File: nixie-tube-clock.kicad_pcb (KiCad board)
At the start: 2 copper layers, 131 parts, among them IC1 TPS61041DBVR, IC2 UCC3803DTR, J5 USB4105-GF-A, J7 DEBUG, Q1 MMBT42, Q2 FDS2672CT, SW1 SW_SPST, U1 CD40109BPW, U2 W25Q32JV, U3 RP2350A, U4 MCP1702T-3302E_CB, U5 CD40109BPW, U6 HV5122PG-G, U7 HV5122PG-G, U8 DS3231M, X1 IQXO-791

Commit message: Add global labels for nets spanning several sheets
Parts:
- moved D12 240.0 mm to (255.5, 98.7)
- moved D11 216.6 mm to (230.1, 98.7)
- moved D10 193.9 mm to (204.7, 98.7)
- moved N6 191.6 mm to (255.5, 98.7)
- moved N4 185.5 mm to (230.1, 98.7)
- moved N2 179.4 mm to (204.7, 98.7)
- moved D9 171.9 mm to (178.8, 99.1)
- moved D8 152.3 mm to (154.0, 99.1)
- moved D7 135.9 mm to (130.6, 99.1)
- moved N5 129.6 mm to (178.8, 99.1)
- moved N3 124.8 mm to (154.0, 99.1)
- moved N1 121.3 mm to (130.6, 99.1)
- moved U6 28.3 mm to (112.6, 106.1)
- moved C34 12.9 mm to (86.4, 46.5), turned to -90 degrees
- moved U8 5.59 mm to (94.0, 48.3)
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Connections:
- N1 pad 1: /nixie_tubes/N1.1 -> N1.1
- U6 pad 36: /nixie_tubes_driver/N1.1 -> N1.1

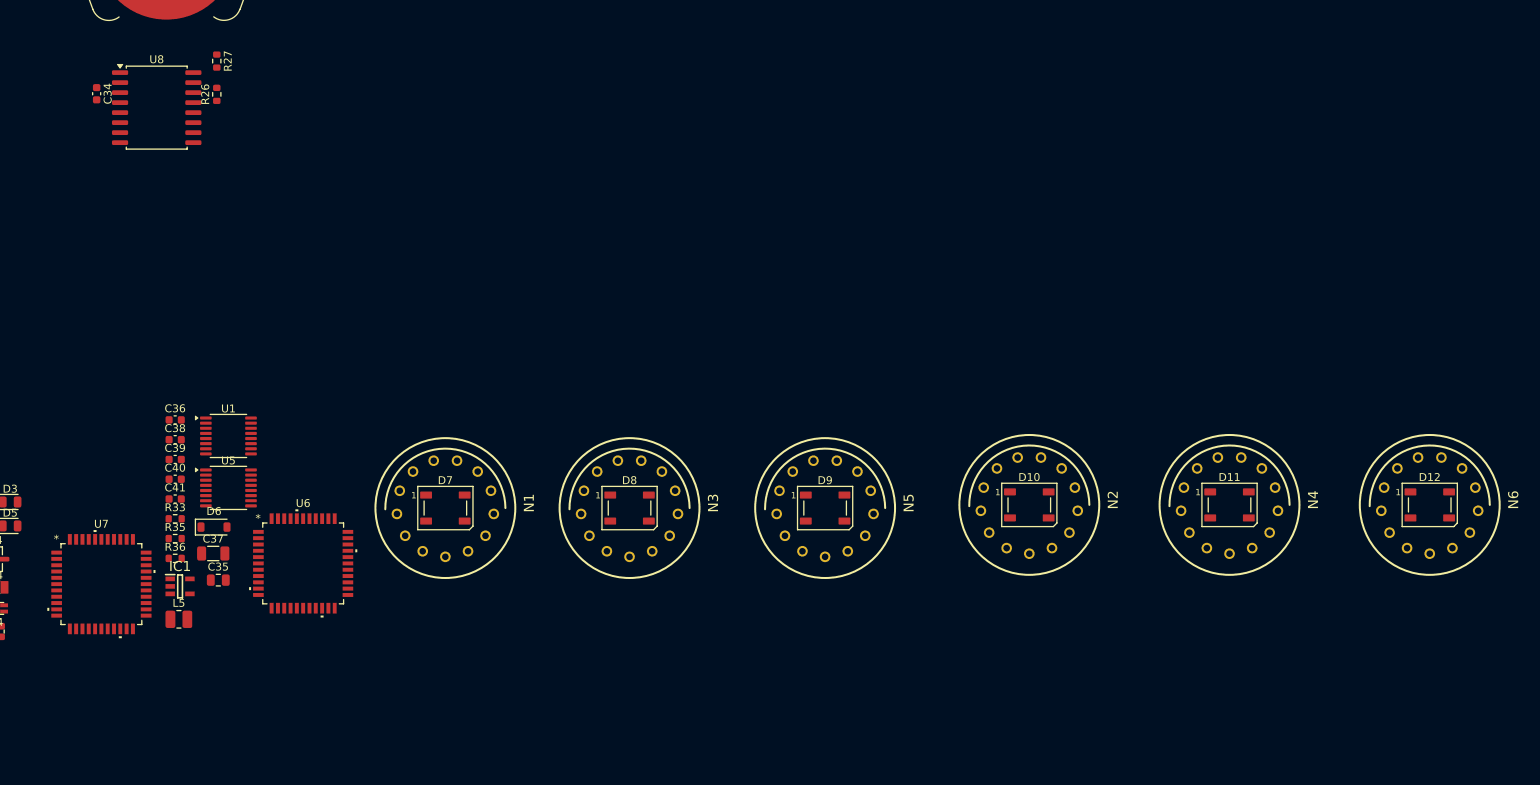
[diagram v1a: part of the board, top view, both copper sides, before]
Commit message: Modify nixie tube nets for easier layout
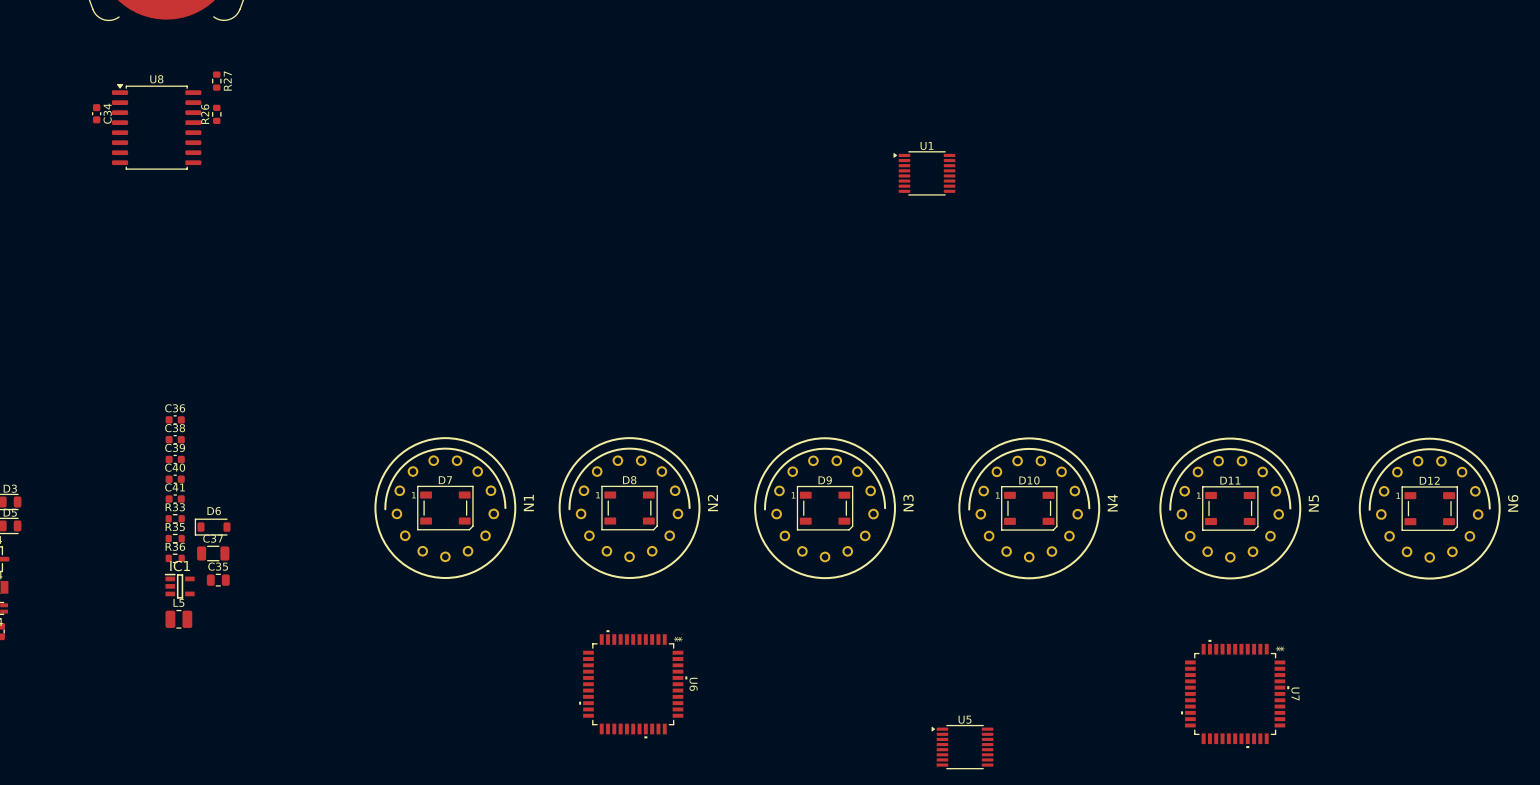
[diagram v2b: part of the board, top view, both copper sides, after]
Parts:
- moved U7 144.5 mm to (230.8, 122.6), turned to -90 degrees
- moved U5 99.1 mm to (196.5, 129.4)
- moved U1 94.7 mm to (191.7, 56.6)
- moved N5 51.4 mm to (230.2, 99.1)
- moved N2 50.7 mm to (154.0, 99.1)
- moved U6 44.6 mm to (154.4, 121.4), turned to -90 degrees
- moved N4 25.4 mm to (204.7, 99.1)
- moved N3 24.8 mm to (178.8, 99.1)
- moved R27 2.54 mm to (101.6, 44.9)
- moved C34 2.54 mm to (86.4, 49.0)
- moved R26 2.54 mm to (101.6, 49.1)
- moved U8 2.54 mm to (94.0, 50.8)
- moved D12 0.47 mm to (255.5, 99.1)
- moved N6 0.47 mm to (255.5, 99.1)
- moved D11 0.46 mm to (230.2, 99.1)
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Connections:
- D7 pad 4: /nixie_tubes/LED_LOGIC_5V -> LED_LOGIC_5V
- N1 pad 0: /nixie_tubes/N1.0 -> N1.0
- N1 pad 2: /nixie_tubes/N1.2 -> N1.2
- N1 pad 3: /nixie_tubes/N1.3 -> N1.3
- N1 pad 4: /nixie_tubes/N1.4 -> N1.4
- N1 pad 5: /nixie_tubes/N1.5 -> N1.5
- N1 pad 6: /nixie_tubes/N1.6 -> N1.6
- N1 pad 7: /nixie_tubes/N1.7 -> N1.7
- N1 pad 8: /nixie_tubes/N1.8 -> N1.8
- N1 pad 9: /nixie_tubes/N1.9 -> N1.9
- N2 pad 0: /nixie_tubes/N2.0 -> N2.0
- N2 pad 1: /nixie_tubes/N2.1 -> N2.1
- N2 pad 2: /nixie_tubes/N2.2 -> N2.2
- N2 pad 3: /nixie_tubes/N2.3 -> N2.3
- N2 pad 4: /nixie_tubes/N2.4 -> N2.4
- N2 pad 5: /nixie_tubes/N2.5 -> N2.5
- N2 pad 6: /nixie_tubes/N2.6 -> N2.6
- N2 pad 7: /nixie_tubes/N2.7 -> N2.7
- N2 pad 8: /nixie_tubes/N2.8 -> N2.8
- N2 pad 9: /nixie_tubes/N2.9 -> N2.9
- N3 pad 0: /nixie_tubes/N3.0 -> N3.0
- N3 pad 1: /nixie_tubes/N3.1 -> N3.1
- N3 pad 2: /nixie_tubes/N3.2 -> N3.2
- N3 pad 3: /nixie_tubes/N3.3 -> N3.3
- N3 pad 4: /nixie_tubes/N3.4 -> N3.4
- N3 pad 5: /nixie_tubes/N3.5 -> N3.5
- N3 pad 6: /nixie_tubes/N3.6 -> N3.6
- N3 pad 7: /nixie_tubes/N3.7 -> N3.7
- N3 pad 8: /nixie_tubes/N3.8 -> N3.8
- N3 pad 9: /nixie_tubes/N3.9 -> N3.9
- N4 pad 0: /nixie_tubes/N4.0 -> N4.0
- N4 pad 1: /nixie_tubes/N4.1 -> N4.1
- N4 pad 2: /nixie_tubes/N4.2 -> N4.2
- N4 pad 3: /nixie_tubes/N4.3 -> N4.3
- N4 pad 4: /nixie_tubes/N4.4 -> N4.4
- N4 pad 5: /nixie_tubes/N4.5 -> N4.5
- N4 pad 6: /nixie_tubes/N4.6 -> N4.6
- N4 pad 7: /nixie_tubes/N4.7 -> N4.7
- N4 pad 8: /nixie_tubes/N4.8 -> N4.8
- N4 pad 9: /nixie_tubes/N4.9 -> N4.9
- N5 pad 0: /nixie_tubes/N5.0 -> N5.0
- N5 pad 1: /nixie_tubes/N5.1 -> N5.1
- N5 pad 2: /nixie_tubes/N5.2 -> N5.2
- N5 pad 3: /nixie_tubes/N5.3 -> N5.3
- N5 pad 4: /nixie_tubes/N5.4 -> N5.4
- N5 pad 5: /nixie_tubes/N5.5 -> N5.5
- N5 pad 6: /nixie_tubes/N5.6 -> N5.6
- N5 pad 7: /nixie_tubes/N5.7 -> N5.7
- N5 pad 8: /nixie_tubes/N5.8 -> N5.8
- N5 pad 9: /nixie_tubes/N5.9 -> N5.9
- N6 pad 0: /nixie_tubes/N6.0 -> N6.0
- N6 pad 1: /nixie_tubes/N6.1 -> N6.1
- N6 pad 2: /nixie_tubes/N6.2 -> N6.2
- N6 pad 3: /nixie_tubes/N6.3 -> N6.3
- N6 pad 4: /nixie_tubes/N6.4 -> N6.4
- N6 pad 5: /nixie_tubes/N6.5 -> N6.5
- N6 pad 6: /nixie_tubes/N6.6 -> N6.6
- N6 pad 7: /nixie_tubes/N6.7 -> N6.7
- N6 pad 8: /nixie_tubes/N6.8 -> N6.8
- N6 pad 9: /nixie_tubes/N6.9 -> N6.9
- R26 pad 2: /real_time_clock/RTC_SDA -> RTC_SDA
- R27 pad 2: /real_time_clock/RTC_SCL -> RTC_SCL
- U1 pad 3: /nixie_tubes_driver/LED_LOGIC_3V3 -> LED_LOGIC_3V3
- U1 pad 4: /nixie_tubes_driver/LED_LOGIC_5V -> LED_LOGIC_5V
- U3 pad 14: /microcontroller/SR_CLK_3V3 -> SR_CLK_3V3
- U3 pad 15: /microcontroller/SR_DATA_IN_3V3 -> SR_DATA_IN_3V3
- U3 pad 16: /microcontroller/SR_STR_3V3 -> SR_STR_3V3
- U3 pad 17: /microcontroller/SR_OE_3V3 -> SR_OE_3V3
- U3 pad 18: /microcontroller/LED_LOGIC_3V3 -> LED_LOGIC_3V3
- U3 pad 2: /microcontroller/RTC_SDA -> RTC_SDA
- U3 pad 3: /microcontroller/RTC_SCL -> RTC_SCL
- U5 pad 10: /nixie_tubes_driver/SR_STR_3V3 -> SR_STR_3V3
- U5 pad 14: /nixie_tubes_driver/SR_OE_3V3 -> SR_OE_3V3
- U5 pad 3: /nixie_tubes_driver/SR_DATA_IN_3V3 -> SR_DATA_IN_3V3
- U5 pad 6: /nixie_tubes_driver/SR_CLK_3V3 -> SR_CLK_3V3
- U6 pad 1: /nixie_tubes_driver/N2.0 -> N2.1
- U6 pad 10: /nixie_tubes_driver/N2.9 -> N2.0
- U6 pad 11: /nixie_tubes_driver/N3.0 -> N1.1
- U6 pad 12: /nixie_tubes_driver/N3.1 -> N1.2
- U6 pad 13: /nixie_tubes_driver/N3.2 -> N1.3
- U6 pad 14: /nixie_tubes_driver/N3.3 -> N1.4
- U6 pad 15: /nixie_tubes_driver/N3.4 -> N1.5
- U6 pad 16: /nixie_tubes_driver/N3.5 -> N1.6
- U6 pad 17: /nixie_tubes_driver/N3.6 -> N1.7
- U6 pad 18: /nixie_tubes_driver/N3.7 -> N1.8
- U6 pad 19: /nixie_tubes_driver/N3.8 -> N1.9
- U6 pad 2: /nixie_tubes_driver/N2.1 -> N2.2
- U6 pad 20: /nixie_tubes_driver/N3.9 -> N1.0
- U6 pad 3: /nixie_tubes_driver/N2.2 -> N2.3
- U6 pad 35: /nixie_tubes_driver/N1.0 -> N3.1
- U6 pad 36: N1.1 -> N3.2
- U6 pad 37: /nixie_tubes_driver/N1.2 -> N3.3
- U6 pad 38: /nixie_tubes_driver/N1.3 -> N3.4
- U6 pad 39: /nixie_tubes_driver/N1.4 -> N3.5
- U6 pad 4: /nixie_tubes_driver/N2.3 -> N2.4
- U6 pad 40: /nixie_tubes_driver/N1.5 -> N3.6
- U6 pad 41: /nixie_tubes_driver/N1.6 -> N3.7
- U6 pad 42: /nixie_tubes_driver/N1.7 -> N3.8
- U6 pad 43: /nixie_tubes_driver/N1.8 -> N3.9
- U6 pad 44: /nixie_tubes_driver/N1.9 -> N3.0
- U6 pad 5: /nixie_tubes_driver/N2.4 -> N2.5
- U6 pad 6: /nixie_tubes_driver/N2.5 -> N2.6
- U6 pad 7: /nixie_tubes_driver/N2.6 -> N2.7
- U6 pad 8: /nixie_tubes_driver/N2.7 -> N2.8
- U6 pad 9: /nixie_tubes_driver/N2.8 -> N2.9
- U7 pad 1: /nixie_tubes_driver/N5.0 -> N5.1
- U7 pad 10: /nixie_tubes_driver/N5.9 -> N5.0
- U7 pad 11: /nixie_tubes_driver/N6.0 -> N4.1
- U7 pad 12: /nixie_tubes_driver/N6.1 -> N4.2
- U7 pad 13: /nixie_tubes_driver/N6.2 -> N4.3
- U7 pad 14: /nixie_tubes_driver/N6.3 -> N4.4
- U7 pad 15: /nixie_tubes_driver/N6.4 -> N4.5
- U7 pad 16: /nixie_tubes_driver/N6.5 -> N4.6
- U7 pad 17: /nixie_tubes_driver/N6.6 -> N4.7
- U7 pad 18: /nixie_tubes_driver/N6.7 -> N4.8
- U7 pad 19: /nixie_tubes_driver/N6.8 -> N4.9
- U7 pad 2: /nixie_tubes_driver/N5.1 -> N5.2
- U7 pad 20: /nixie_tubes_driver/N6.9 -> N4.0
- U7 pad 3: /nixie_tubes_driver/N5.2 -> N5.3
- U7 pad 35: /nixie_tubes_driver/N4.0 -> N6.1
- U7 pad 36: /nixie_tubes_driver/N4.1 -> N6.2
- U7 pad 37: /nixie_tubes_driver/N4.2 -> N6.3
- U7 pad 38: /nixie_tubes_driver/N4.3 -> N6.4
- U7 pad 39: /nixie_tubes_driver/N4.4 -> N6.5
- U7 pad 4: /nixie_tubes_driver/N5.3 -> N5.4
- U7 pad 40: /nixie_tubes_driver/N4.5 -> N6.6
- U7 pad 41: /nixie_tubes_driver/N4.6 -> N6.7
- U7 pad 42: /nixie_tubes_driver/N4.7 -> N6.8
- U7 pad 43: /nixie_tubes_driver/N4.8 -> N6.9
- U7 pad 44: /nixie_tubes_driver/N4.9 -> N6.0
- U7 pad 5: /nixie_tubes_driver/N5.4 -> N5.5
- U7 pad 6: /nixie_tubes_driver/N5.5 -> N5.6
- U7 pad 7: /nixie_tubes_driver/N5.6 -> N5.7
- U7 pad 8: /nixie_tubes_driver/N5.7 -> N5.8
- U7 pad 9: /nixie_tubes_driver/N5.8 -> N5.9
- U8 pad 15: /real_time_clock/RTC_SDA -> RTC_SDA
- U8 pad 16: /real_time_clock/RTC_SCL -> RTC_SCL

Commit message: Begin positioning and grouping components
Add bypass caps to level shifters Vdd
Rearrange pins on shift register
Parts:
- added C48: 0.1uF, Capacitor_SMD:C_0603_1608Metric, F.Cu at (195.8, 62.7)
- added C49: 0.1uF, Capacitor_SMD:C_0603_1608Metric, F.Cu at (111.5, 105.4)
- added H1: MountingHole, MountingHole:MountingHole_3.2mm_M3, F.Cu at (84.0, 26.4)
- added H2: MountingHole, MountingHole:MountingHole_3.2mm_M3, F.Cu at (84.0, 34.3)
- added H3: MountingHole, MountingHole:MountingHole_3.2mm_M3, F.Cu at (84.0, 42.3)
- added H4: MountingHole, MountingHole:MountingHole_3.2mm_M3, F.Cu at (84.0, 50.2)
- moved R34 229.8 mm to (255.6, 114.9), turned to 90 degrees
- moved R42 225.6 mm to (255.6, 120.0), turned to 90 degrees
- moved C47 212.1 mm to (257.3, 102.6), turned to 180 degrees
- moved R32 205.4 mm to (230.1, 115.1), turned to 90 degrees
- moved R41 201.5 mm to (230.1, 120.1), turned to 90 degrees
- moved C46 187.6 mm to (231.9, 102.6), turned to 180 degrees
- moved R31 181.6 mm to (204.7, 115.1), turned to 90 degrees
- moved R40 178.0 mm to (204.7, 120.1), turned to 90 degrees
- moved D4 165.6 mm to (220.4, 35.2), turned to -90 degrees
- moved J5 164.1 mm to (191.5, 22.3), turned to 180 degrees
- moved R21 163.8 mm to (217.4, 33.0)
- moved R22 163.8 mm to (217.4, 35.5)
- moved R23 163.8 mm to (217.4, 38.0)
- moved C45 163.3 mm to (206.5, 102.6), turned to 180 degrees
- moved C34 162.3 mm to (248.7, 47.7), turned to 90 degrees
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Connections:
- U6 pad 1: N2.1 -> N2.0
- U6 pad 10: N2.0 -> N2.1
- U6 pad 11: N1.1 -> N3.0
- U6 pad 12: N1.2 -> N3.9
- U6 pad 13: N1.3 -> N3.8
- U6 pad 14: N1.4 -> N3.7
- U6 pad 15: N1.5 -> N3.6
- U6 pad 16: N1.6 -> N3.5
- U6 pad 17: N1.7 -> N3.4
- U6 pad 18: N1.8 -> N3.3
- U6 pad 19: N1.9 -> N3.2
- U6 pad 2: N2.2 -> N2.9
- U6 pad 20: N1.0 -> N3.1
- U6 pad 3: N2.3 -> N2.8
- U6 pad 35: N3.1 -> N1.0
- U6 pad 36: N3.2 -> N1.9
- U6 pad 37: N3.3 -> N1.8
- U6 pad 38: N3.4 -> N1.7
- U6 pad 39: N3.5 -> N1.6
- U6 pad 4: N2.4 -> N2.7
- U6 pad 40: N3.6 -> N1.5
- U6 pad 41: N3.7 -> N1.4
- U6 pad 42: N3.8 -> N1.3
- U6 pad 43: N3.9 -> N1.2
- U6 pad 44: N3.0 -> N1.1
- U6 pad 5: N2.5 -> N2.6
- U6 pad 6: N2.6 -> N2.5
- U6 pad 7: N2.7 -> N2.4
- U6 pad 8: N2.8 -> N2.3
- U6 pad 9: N2.9 -> N2.2
- U7 pad 1: N5.1 -> N5.0
- U7 pad 10: N5.0 -> N5.1
- U7 pad 11: N4.1 -> N6.0
- U7 pad 12: N4.2 -> N6.9
- U7 pad 13: N4.3 -> N6.8
- U7 pad 14: N4.4 -> N6.7
- U7 pad 15: N4.5 -> N6.6
- U7 pad 16: N4.6 -> N6.5
- U7 pad 17: N4.7 -> N6.4
- U7 pad 18: N4.8 -> N6.3
- U7 pad 19: N4.9 -> N6.2
- U7 pad 2: N5.2 -> N5.9
- U7 pad 20: N4.0 -> N6.1
- U7 pad 3: N5.3 -> N5.8
- U7 pad 35: N6.1 -> N4.0
- U7 pad 36: N6.2 -> N4.9
- U7 pad 37: N6.3 -> N4.8
- U7 pad 38: N6.4 -> N4.7
- U7 pad 39: N6.5 -> N4.6
- U7 pad 4: N5.4 -> N5.7
- U7 pad 40: N6.6 -> N4.5
- U7 pad 41: N6.7 -> N4.4
- U7 pad 42: N6.8 -> N4.3
- U7 pad 43: N6.9 -> N4.2
- U7 pad 44: N6.0 -> N4.1
- U7 pad 5: N5.5 -> N5.6
- U7 pad 6: N5.6 -> N5.5
- U7 pad 7: N5.7 -> N5.4
- U7 pad 8: N5.8 -> N5.3
- U7 pad 9: N5.9 -> N5.2
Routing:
- net N2.8: track 0.00 -> 1.02 mm

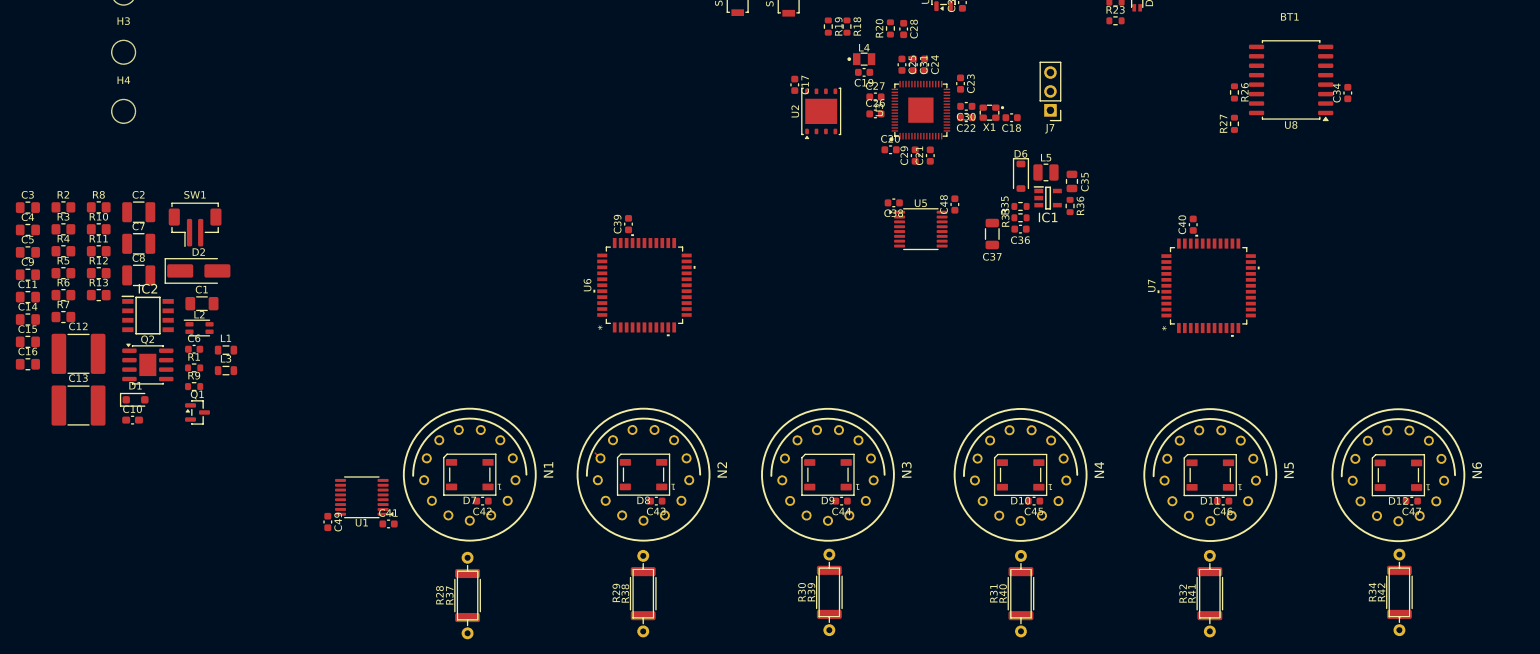
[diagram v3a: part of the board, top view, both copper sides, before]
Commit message: add power supply layout
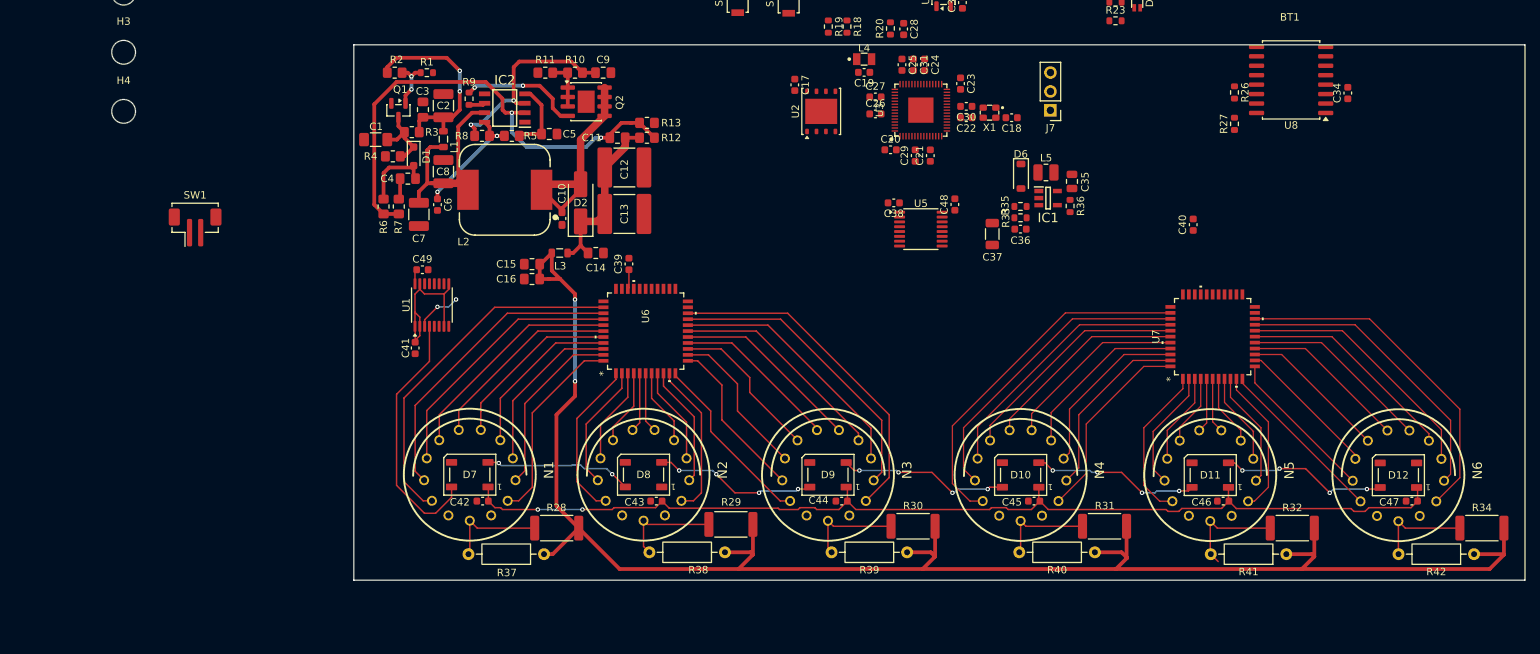
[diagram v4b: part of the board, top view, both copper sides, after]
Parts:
- L2: footprint Inductor_SMD:L_CommonMode_Wurth_WE-CNSW-1206 -> eclectronics_nixie_footprints:WE-PD_1210
- moved C11 82.1 mm to (150.5, 53.8), turned to 180 degrees
- moved C9 82.0 mm to (148.5, 45.0)
- moved C13 77.8 mm to (151.4, 64.0)
- moved C12 77.6 mm to (151.4, 57.8)
- moved R13 77.3 mm to (154.4, 51.8)
- moved C14 76.9 mm to (147.5, 69.2)
- moved R12 75.9 mm to (154.4, 53.8)
- moved C5 71.9 mm to (141.3, 53.2)
- moved Q2 68.8 mm to (146.2, 48.9)
- moved C16 68.8 mm to (139.0, 72.8), turned to 180 degrees
- moved C15 68.6 mm to (139.0, 70.8), turned to 180 degrees
- moved R10 67.4 mm to (144.8, 45.0)
- moved R11 64.7 mm to (140.8, 45.0), turned to 180 degrees
- moved C10 63.8 mm to (143.0, 64.6), turned to -90 degrees
- moved R5 63.1 mm to (136.2, 53.5), turned to 180 degrees
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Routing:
- net +160V: track 0.00 -> 231.2 mm, vias 0 -> 2
- net +5V: track 0.00 -> 168.5 mm, vias 0 -> 4
- net Net-(IC2-FB): track 0.00 -> 67.2 mm, vias 0 -> 2
- net N4.0: track 0.00 -> 48.4 mm
- net N1.0: track 0.00 -> 47.9 mm
- net N6.1: track 0.00 -> 46.3 mm
- net N3.1: track 0.00 -> 45.6 mm
- net N4.9: track 0.00 -> 41.6 mm
- net N1.9: track 0.00 -> 41.0 mm
- net N3.2: track 0.00 -> 40.2 mm
- net N6.2: track 0.00 -> 40.1 mm
- net N4.8: track 0.00 -> 35.9 mm
- net N1.8: track 0.00 -> 35.3 mm
- net N6.3: track 0.00 -> 34.5 mm
- net LED_LOGIC_5V: track 0.00 -> 34.5 mm
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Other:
- board outline added: 157.5 x 72 mm

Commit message: Begin layout of microcontroller components
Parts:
- L2: footprint eclectronics_nixie_footprints:WE-PD_1210 -> Inductor_SMD:L_CommonMode_Wurth_WE-CNSW-1206
- R33: footprint Resistor_SMD:R_0603_1608Metric -> Resistor_SMD:R_0805_2012Metric
- moved J7 55.1 mm to (259.1, 72.4)
- moved C35 53.6 mm to (264.4, 50.3)
- moved D6 53.6 mm to (257.5, 49.6)
- moved R33 53.6 mm to (257.4, 55.2)
- moved R35 53.6 mm to (257.4, 53.6)
- moved C36 53.6 mm to (257.4, 56.7)
- moved C37 53.6 mm to (253.6, 57.4)
- moved IC1 53.6 mm to (261.2, 52.5)
- moved L5 53.6 mm to (260.9, 49.1)
- moved R36 53.6 mm to (264.1, 53.6)
- moved S1 51.6 mm to (208.1, 73.6)
- moved R14 51.6 mm to (208.1, 70.3), turned to 180 degrees
- moved R15 42.1 mm to (171.5, 73.8)
- moved C34 41.8 mm to (213.7, 70.6), turned to 0 degrees
- moved S2 35.7 mm to (172.2, 70.5), turned to -90 degrees
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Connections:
- U3 pad 2: RTC_SDA -> unconnected-(U3-GPIO0-Pad2)
- U3 pad 27: unconnected-(U3-GPIO16-Pad27) -> RTC_SDA
- U3 pad 28: unconnected-(U3-GPIO17-Pad28) -> RTC_SCL
- U3 pad 3: RTC_SCL -> unconnected-(U3-GPIO1-Pad3)
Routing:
- net Net-(BT1-+): track 0.00 -> 59.8 mm
- net GND: track 0.00 -> 43.7 mm
- net +3V3: track 0.00 -> 24.0 mm
- net RTC_SDA: track 0.00 -> 23.6 mm
- net RTC_SCL: track 0.00 -> 21.3 mm
- net /microcontroller/BOOT: track 0.00 -> 20.3 mm
- net +1V1: track 0.00 -> 15.0 mm
- net Net-(U2-~{HOLD}/IO3): track 0.00 -> 13.7 mm
- net /microcontroller/RUN: track 0.00 -> 13.5 mm
- net Net-(U2-SCK): track 0.00 -> 12.4 mm
- net +5V: track 168.5 -> 180.8 mm
- net Net-(U2-DO/IO1): track 0.00 -> 11.6 mm
- net Net-(U2-DI/IO0): track 0.00 -> 10.7 mm
- net Net-(U2-~{WP}/IO2): track 0.00 -> 10.2 mm
- net Net-(U3-USB_D+): track 0.00 -> 6.67 mm
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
